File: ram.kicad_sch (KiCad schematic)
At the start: 33 parts, among them IC11 HM514260AZ8, IC21 HM514260AJ8, IC22 HM514260AJ8, IC25 74HC139, IC6 HM514260AZ8

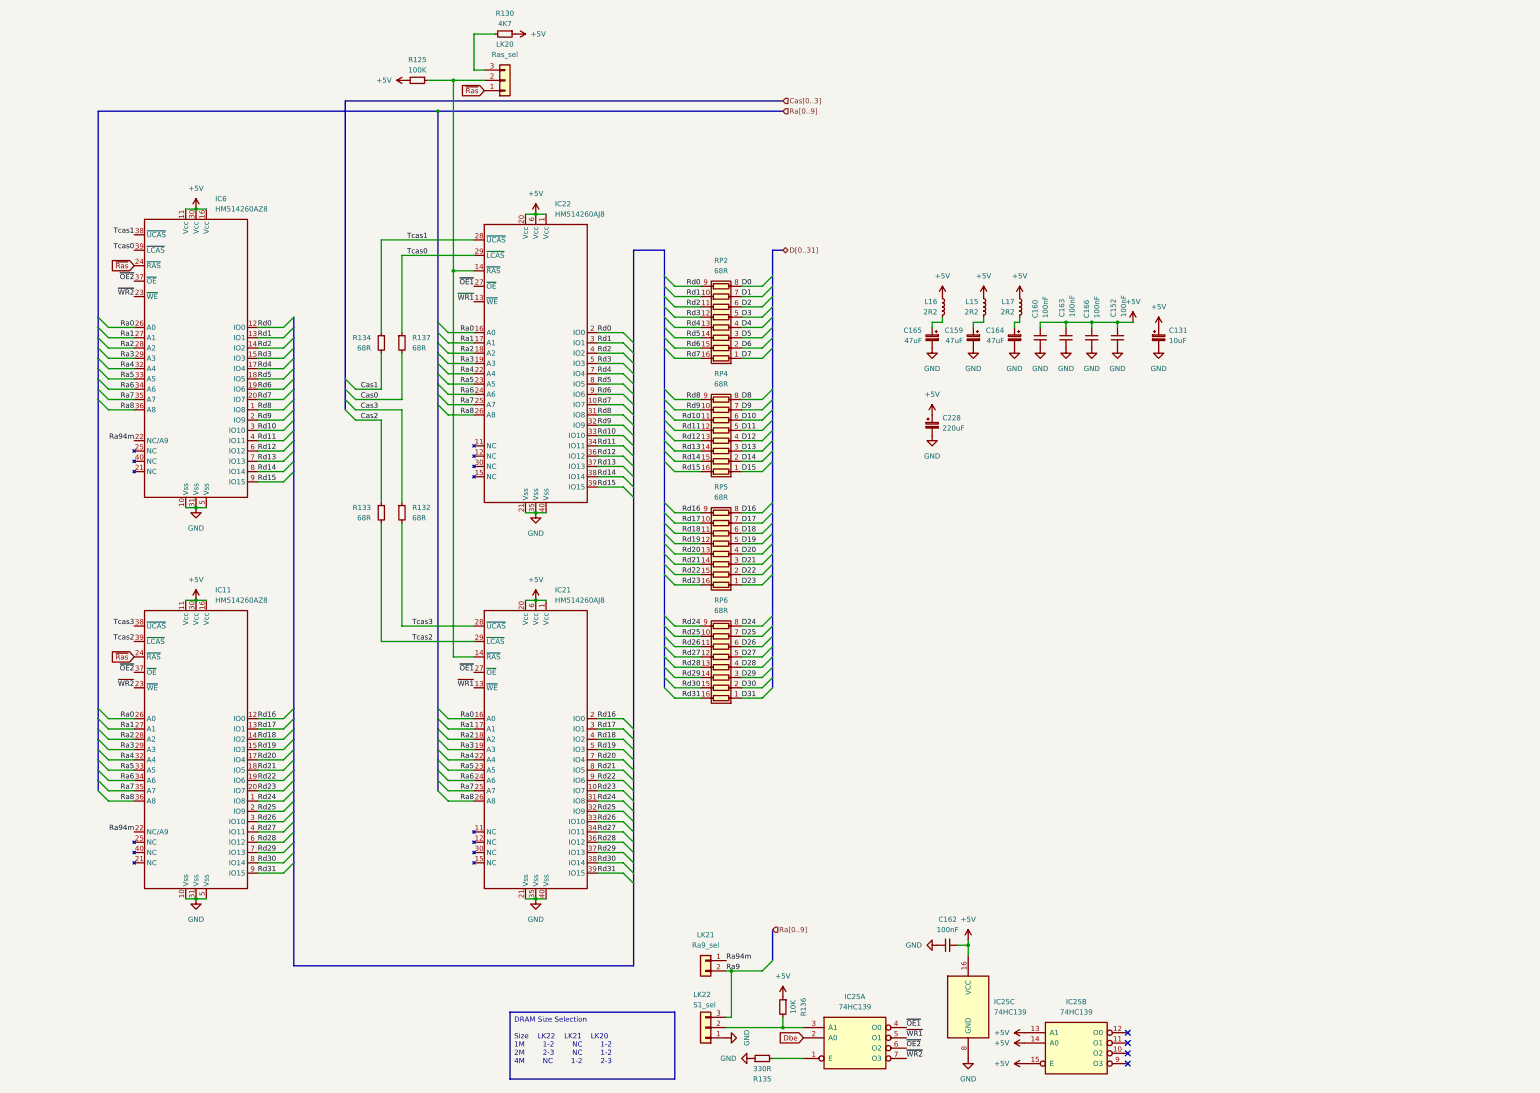
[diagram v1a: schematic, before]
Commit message: add ide and rework onboard ram
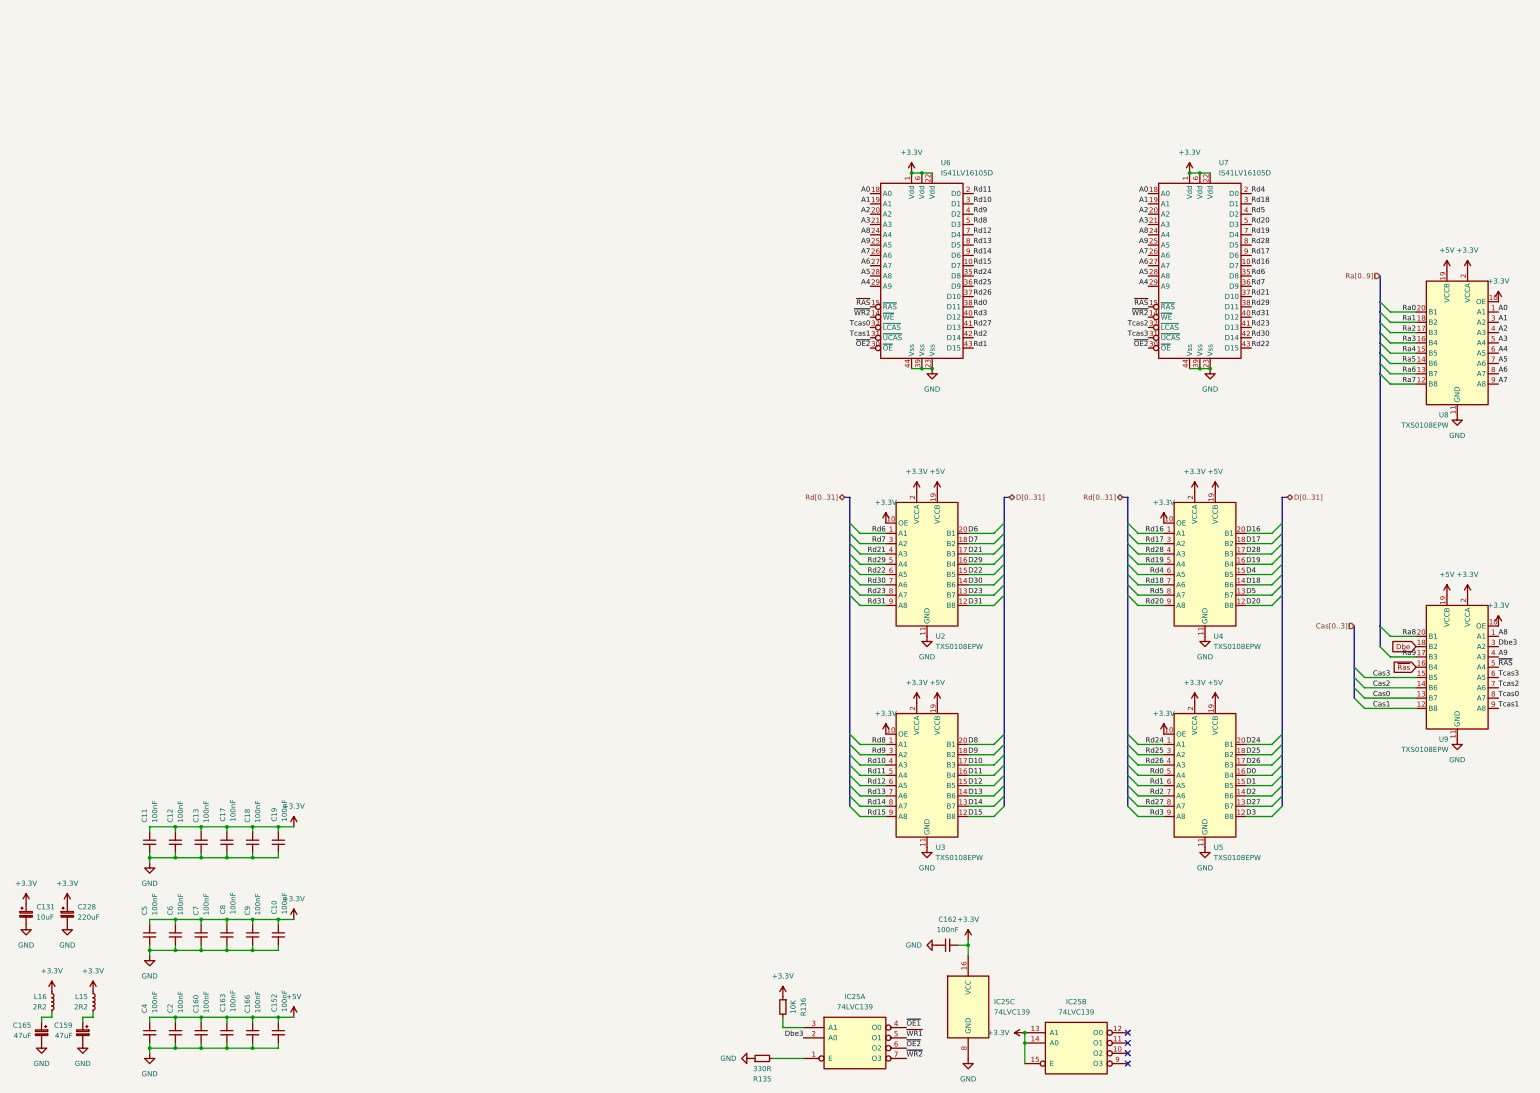
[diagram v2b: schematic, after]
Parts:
- removed C164: 47uF, Capacitor_THT:CP_Axial_L11.0mm_D6.0mm_P18.00mm_Horizontal, symbol Device:C_Polarized_Small
- removed IC11, IC6: HM514260AZ8, Acorn:ZIP-40, symbol Acorn:HM514260AZ
- removed IC21, IC22: HM514260AJ8, Acorn:SOJ-40_10.16mm_P1.27mm, symbol Acorn:HM514260AJ
- removed L17: 2R2, Acorn:L_Acorn_8x3mm, symbol Device:L_Small
- removed LK20: Ras_sel, Connector_PinHeader_2.54mm:PinHeader_1x03_P2.54mm_Vertical, symbol Connector_Generic:Conn_01x03
- removed LK21: Ra9_sel, Connector_PinHeader_2.54mm:PinHeader_1x02_P2.54mm_Vertical, symbol Connector_Generic:Conn_01x02
- removed LK22: S1_sel, Connector_PinHeader_2.54mm:PinHeader_1x03_P2.54mm_Vertical, symbol Connector_Generic:Conn_01x03
- removed R125: 100K, Resistor_SMD:R_0805_2012Metric, symbol Device:R_Small
- removed R130: 4K7, Resistor_SMD:R_0805_2012Metric, symbol Device:R_Small
- removed R132, R133, R134, R137: 68R, Resistor_SMD:R_0805_2012Metric, symbol Device:R_Small
- removed RP2, RP4, RP5, RP6: 68R, Package_SO:SOIC-16W_5.3x10.2mm_P1.27mm, symbol Device:R_Pack08
- added C10, C11, C12, C13, C17, C18, C19, C2, C4, C5, C6, C7, C8, C9: 100nF, Capacitor_SMD:C_0805_2012Metric, symbol Device:C_Small
- added U2, U3, U4, U5, U8, U9: TXS0108EPW, Package_SO:TSSOP-20_4.4x6.5mm_P0.65mm, symbol Logic_LevelTranslator:TXS0108EPW
- added U6, U7: IS41LV16105D, Acorn:TSOP-II-44-50, symbol Acorn:IS41LV16105D
- IC25: value 74HC139 -> 74LVC139; footprint Package_SO:SOIC-16_3.9x9.9mm_P1.27mm -> Package_SO:TSSOP-16_4.4x5mm_P0.65mm
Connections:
- net +5V: now also C2.1, C4.1, U2.19 (VCCB), U3.19 (VCCB), U4.19 (VCCB), U5.19 (VCCB), U8.19 (VCCB), U9.19 (VCCB); no longer C131.1, C162.2, C228.1, IC25.13 (A1), IC25.14 (A0), IC25.15 (E), IC25.16 (VCC), L15.1, L16.1, R136.1
- net Cas0: now also U9.13 (B7)
- net Cas1: now also U9.12 (B8)
- net Cas2: now also U9.14 (B6)
- net Cas3: now also U9.15 (B5)
- net D0: now also U5.16 (B4)
- net D1: now also U5.15 (B5)
- net D10: now also U3.17 (B3)
- net D11: now also U3.16 (B4)
- net D12: now also U3.15 (B5)
- net D13: now also U3.14 (B6)
- net D14: now also U3.13 (B7)
- net D15: now also U3.12 (B8)
- net D16: now also U4.20 (B1)
- net D17: now also U4.18 (B2)
- net D18: now also U4.14 (B6)
- net D19: now also U4.16 (B4)
- net D2: now also U5.14 (B6)
- net D20: now also U4.12 (B8)
- net D21: now also U2.17 (B3)
- net D22: now also U2.15 (B5)
- net D23: now also U2.13 (B7)
- net D24: now also U5.20 (B1)
- net D25: now also U5.18 (B2)
- net D26: now also U5.17 (B3)
- net D27: now also U5.13 (B7)
- net D28: now also U4.17 (B3)
- net D29: now also U2.16 (B4)
- net D3: now also U5.12 (B8)
- net D30: now also U2.14 (B6)
- net D31: now also U2.12 (B8)
- net D4: now also U4.15 (B5)
- net D5: now also U4.13 (B7)
- net D6: now also U2.20 (B1)
- net D7: now also U2.18 (B2)
- net D8: now also U3.20 (B1)
- net D9: now also U3.18 (B2)
- net Dbe: now also U9.18 (B2); no longer IC25.2 (A0)
- net GND: now also C10.2, C11.2, C12.2, C13.2, C17.2, C18.2, C19.2, C2.2, C4.2, C5.2, C6.2, C7.2, C8.2, C9.2, U2.11 (GND), U3.11 (GND), U4.11 (GND), U5.11 (GND), U6.23 (Vss), U6.39 (Vss), U6.44 (Vss), U7.23 (Vss), U7.39 (Vss), U7.44 (Vss), U8.11 (GND), U9.11 (GND)
- net Ra0: now also U8.20 (B1)
- net Ra1: now also U8.18 (B2)
- net Ra2: now also U8.17 (B3)
- net Ra3: now also U8.16 (B4)
- net Ra4: now also U8.15 (B5)
- net Ra5: now also U8.14 (B6)
- net Ra6: now also U8.13 (B7)
- net Ra7: now also U8.12 (B8)
- net Ra8: now also U9.20 (B1)
- net Ra9: now also U9.17 (B3)
- net Rd0: now also U5.5 (A4), U6.38 (D11)
- net Rd1: now also U5.6 (A5), U6.43 (D15)
- net Rd10: now also U3.4 (A3), U6.3 (D1)
- net Rd11: now also U3.5 (A4), U6.2 (D0)
- net Rd12: now also U3.6 (A5), U6.7 (D4)
- net Rd13: now also U3.7 (A6), U6.8 (D5)
- net Rd14: now also U3.8 (A7), U6.9 (D6)
- net Rd15: now also U3.9 (A8), U6.10 (D7)
- net Rd16: now also U4.1 (A1), U7.10 (D7)
- net Rd17: now also U4.3 (A2), U7.9 (D6)
- net Rd18: now also U4.7 (A6), U7.3 (D1)
- net Rd19: now also U4.5 (A4), U7.7 (D4)
- net Rd2: now also U5.7 (A6), U6.42 (D14)
- net Rd20: now also U4.9 (A8), U7.5 (D3)
- net Rd21: now also U2.4 (A3), U7.37 (D10)
- net Rd22: now also U2.6 (A5), U7.43 (D15)
- net Rd23: now also U2.8 (A7), U7.41 (D13)
- net Rd24: now also U5.1 (A1), U6.35 (D8)
- net Rd25: now also U5.3 (A2), U6.36 (D9)
- net Rd26: now also U5.4 (A3), U6.37 (D10)
- net Rd27: now also U5.8 (A7), U6.41 (D13)
- net Rd28: now also U4.4 (A3), U7.8 (D5)
- net Rd29: now also U2.5 (A4), U7.38 (D11)
- net Rd3: now also U5.9 (A8), U6.40 (D12)
- net Rd30: now also U2.7 (A6), U7.42 (D14)
- net Rd31: now also U2.9 (A8), U7.40 (D12)
- net Rd4: now also U4.6 (A5), U7.2 (D0)
- net Rd5: now also U4.8 (A7), U7.4 (D2)
- net Rd6: now also U2.1 (A1), U7.35 (D8)
- net Rd7: now also U2.3 (A2), U7.36 (D9)
- net Rd8: now also U3.1 (A1), U6.5 (D3)
- net Rd9: now also U3.3 (A2), U6.4 (D2)
- net Tcas0: now also U6.32 (~{LCAS}), U9.8 (A7)
- net Tcas1: now also U6.31 (~{UCAS}), U9.9 (A8)
- net Tcas2: now also U7.32 (~{LCAS}), U9.7 (A6)
- net Tcas3: now also U7.31 (~{UCAS}), U9.6 (A5)
- net ~{OE2}: now also U6.30 (~{OE}), U7.30 (~{OE})
- net ~{Ras}: now also U9.16 (B4)
- net ~{WR2}: now also U6.14 (~{WE}), U7.14 (~{WE})
- new net: U7.11 (NC), U7.12 (NC), U7.13 (NC), U7.16 (NC), U7.17 (NC), U7.33 (NC), U7.34 (NC)
- new net: U6.11 (NC), U6.12 (NC), U6.13 (NC), U6.16 (NC), U6.17 (NC), U6.33 (NC), U6.34 (NC)
- new net +3.3V: C10.1, C11.1, C12.1, C13.1, C131.1, C162.2, C17.1, C18.1, C19.1, C228.1, C5.1, C6.1, C7.1, C8.1, C9.1, IC25.13 (A1), IC25.14 (A0), IC25.15 (E), IC25.16 (VCC), L15.1, L16.1, R136.1, U2.10 (OE), U2.2 (VCCA), U3.10 (OE), U3.2 (VCCA), U4.10 (OE), U4.2 (VCCA), U5.10 (OE), U5.2 (VCCA), U6.1 (Vdd), U6.22 (Vdd), U6.6 (Vdd), U7.1 (Vdd), U7.22 (Vdd), U7.6 (Vdd), U8.10 (OE), U8.2 (VCCA), U9.10 (OE), U9.2 (VCCA)
- new net A0: U6.18 (A0), U7.18 (A0), U8.1 (A1)
- new net A1: U6.19 (A1), U7.19 (A1), U8.3 (A2)
- new net A2: U6.20 (A2), U7.20 (A2), U8.4 (A3)
- new net A3: U6.21 (A3), U7.21 (A3), U8.5 (A4)
- new net A4: U6.29 (A9), U7.29 (A9), U8.6 (A5)
- new net A5: U6.28 (A8), U7.28 (A8), U8.7 (A6)
- new net A6: U6.27 (A7), U7.27 (A7), U8.8 (A7)
- new net A7: U6.26 (A6), U7.26 (A6), U8.9 (A8)
- new net A8: U6.24 (A4), U7.24 (A4), U9.1 (A1)
- new net A9: U6.25 (A5), U7.25 (A5), U9.4 (A3)
- new net Dbe3: IC25.2 (A0), U9.3 (A2)
- new net ~{RAS}: U6.15 (~{RAS}), U7.15 (~{RAS}), U9.5 (A4)
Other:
- moved on the sheet: C131, C152, C159, C160, C163, C165, C166, C228, L15, L16
